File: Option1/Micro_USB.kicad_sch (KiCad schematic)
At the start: 10 parts, among them J1401 10118194-0001LF, U1401 CH340X

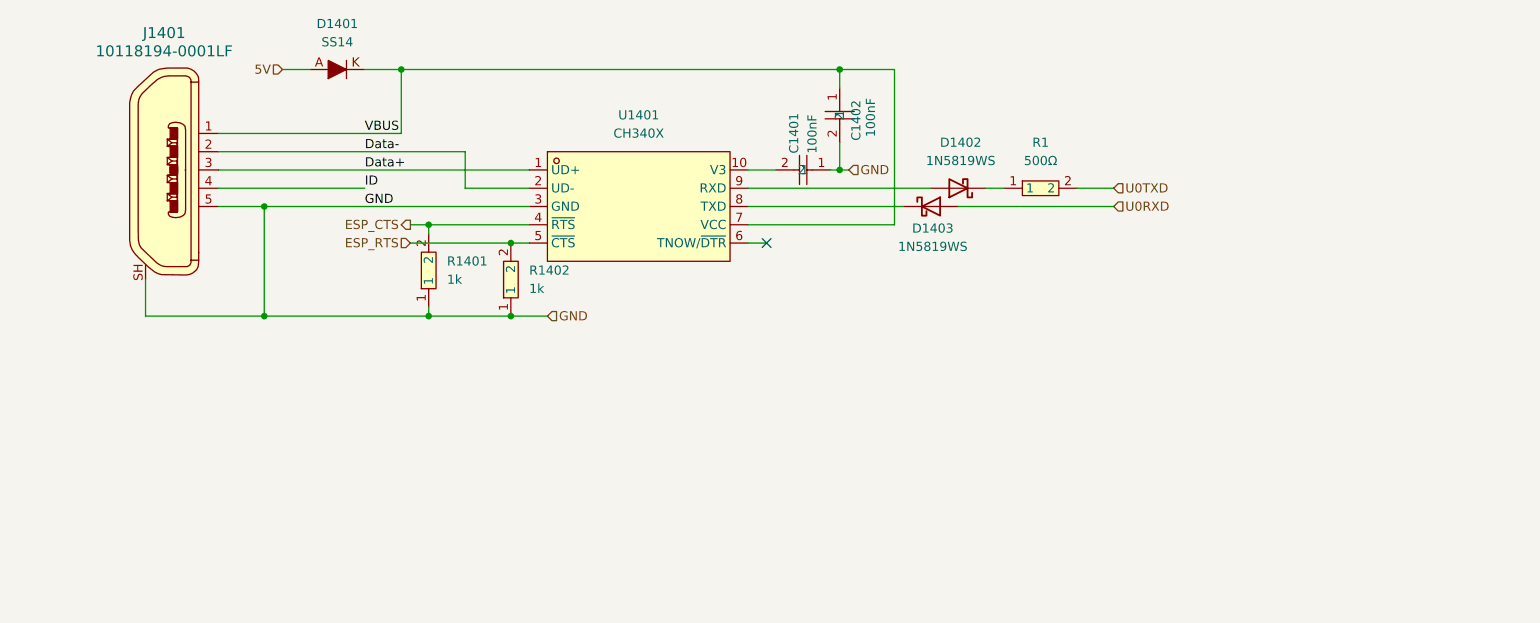
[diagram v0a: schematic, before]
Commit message: SPI Flash hinzugefügt, IN/Outputs vereinheitlicht, USB Flash Möglichkeit hinzugefügt, Display fehtl noch
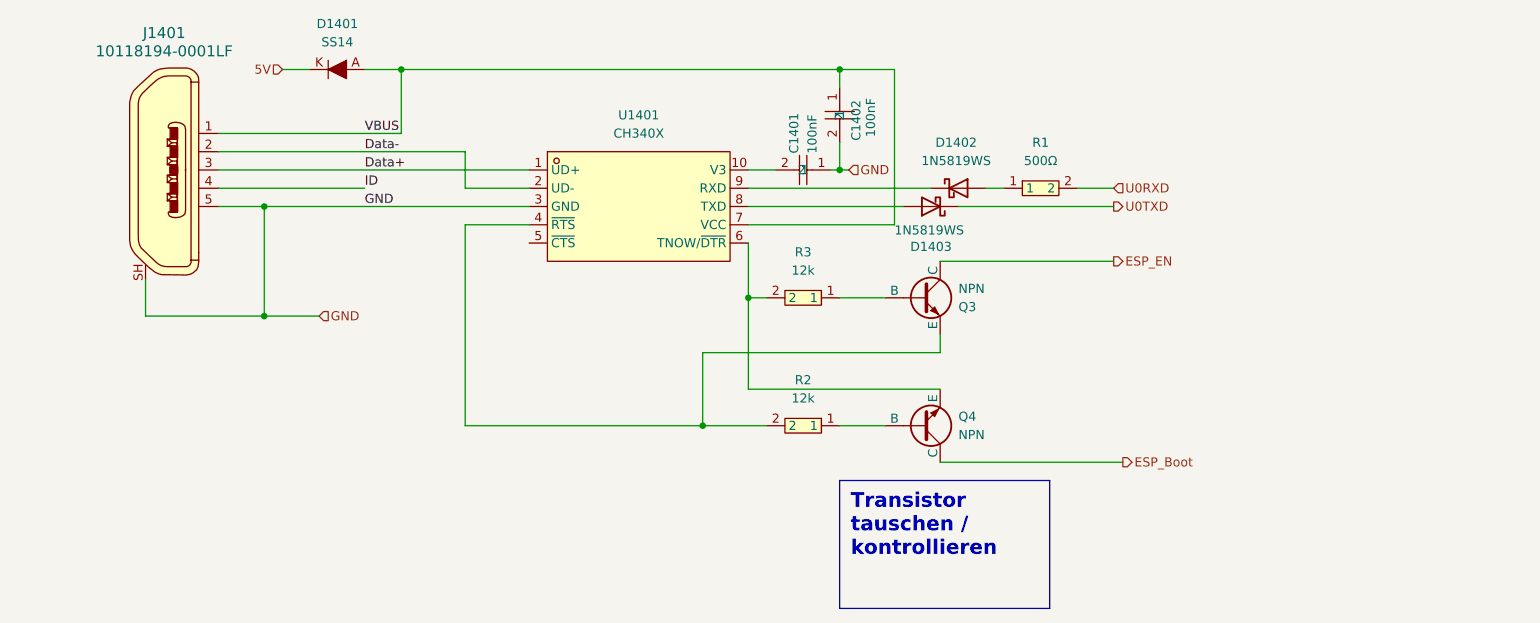
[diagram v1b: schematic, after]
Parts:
- removed R1401, R1402: 1k, easyeda2kicad:R0603, symbol easyeda2kicad:0603WAF1001T5E
- added Q3, Q4: NPN, symbol Simulation_SPICE:NPN
- added R2, R3: 12k, easyeda2kicad:R0603, symbol easyeda2kicad:0603WAF1202T5E
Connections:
- net 5V: now also D1401.K; no longer D1401.A
- net U0RXD: now also R1.2; no longer D1403.2 (A)
- net U0TXD: now also D1403.1 (K); no longer R1.2
- net VBUS: now also D1401.A; no longer D1401.K
- net at R1.1: now also D1402.2 (A); no longer D1402.1 (K)
- net at U1401.6 (TNOW/~{DTR}): now also Q4.3 (E), R3.2
- net at U1401.8 (TXD): now also D1403.2 (A); no longer D1403.1 (K)
- net at U1401.9 (RXD): now also D1402.1 (K); no longer D1402.2 (A)
- net ESP_CTS: no longer names the net of U1401.4 (~{RTS})
- net ESP_CTS: now also Q3.3 (E), R2.2
- net ESP_RTS: no longer names the net of U1401.5 (~{CTS})
- new net: Q3.2 (B), R3.1
- new net: Q4.2 (B), R2.1
- new net ESP_Boot: Q4.1 (C)
- new net ESP_EN: Q3.1 (C)
- no-connect marks 1 -> 0
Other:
- moved on the sheet: D1401, D1402, D1403

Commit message: Added Export for Review 1
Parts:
- renumbered Q3 to Q1401, Q4 to Q1402
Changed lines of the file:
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@@
 		(dnp no)
 		(fields_autoplaced yes)
-		(property "Reference" "Q3"
-			(at 149.86 69.8501 0)
+		(property "Reference" "Q1401"
+			(at 149.86 67.3099 0)
 			(effects
 				(font
@@
 		)
 		(property "Value" "NPN"
-			(at 149.86 67.3101 0)
+			(at 149.86 69.8499 0)
 			(effects
 				(font
@@
 			(project ""
 				(path "/b9e5f262-9648-4b79-bdd1-af888b822329/38430192-9545-4dc5-9188-f56f0a78c828"
-					(reference "Q3")
+					(reference "Q1401")
 					(unit 1)
 				)
@@
 		(dnp no)
 		(fields_autoplaced yes)
-		(property "Reference" "Q4"
+		(property "Reference" "Q1402"
 			(at 149.86 85.0899 0)
 			(effects
@@
 			(project ""
 				(path "/b9e5f262-9648-4b79-bdd1-af888b822329/38430192-9545-4dc5-9188-f56f0a78c828"
-					(reference "Q4")
+					(reference "Q1402")
 					(unit 1)
 				)

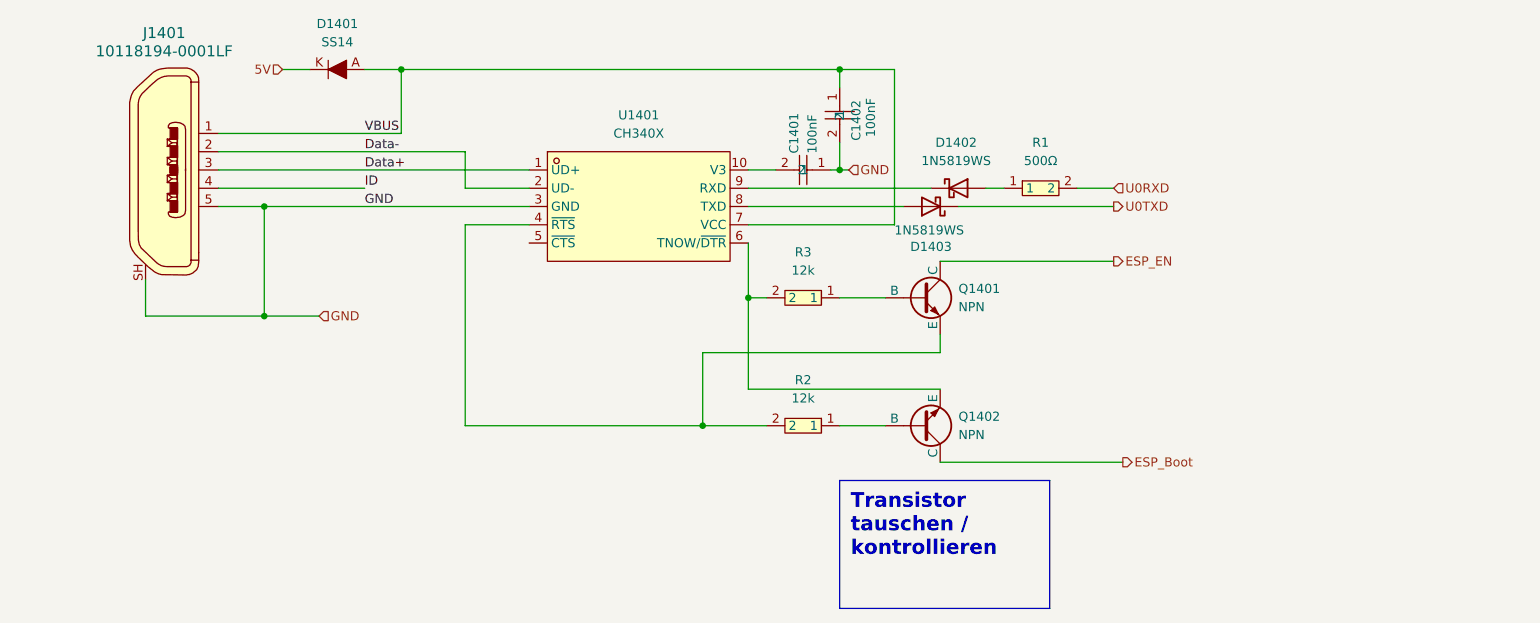
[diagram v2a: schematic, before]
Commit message: USB auf 3V3 umgebaut
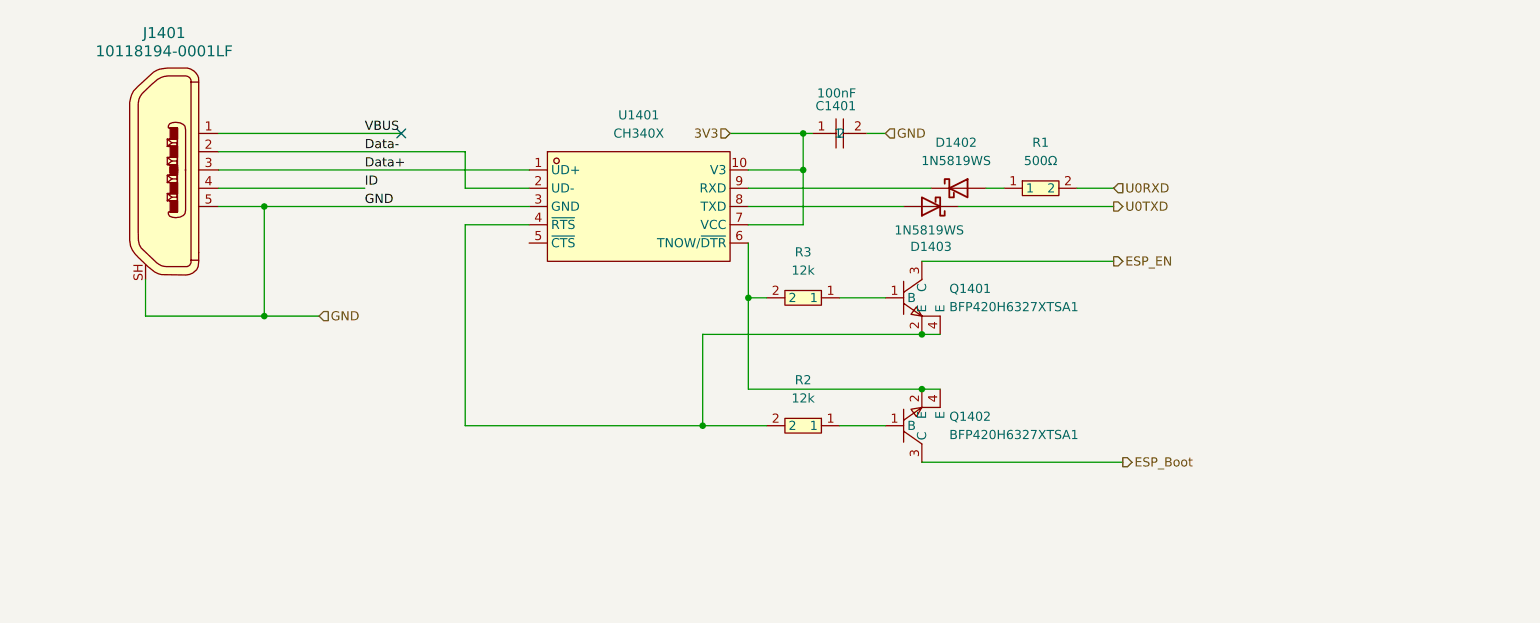
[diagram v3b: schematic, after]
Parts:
- removed C1401: 100nF, easyeda2kicad:C0603, symbol easyeda2kicad:CL10B104KA8NNNC
- removed D1401: SS14, digikey-footprints:DO-214AC, symbol dk_Diodes-Rectifiers-Single:SS14
- removed Q1401, Q1402: NPN, symbol Simulation_SPICE:NPN
- added Q1401, Q1402: BFP420H6327XTSA1, easyeda2kicad:SOT343_L2.0-W1.3-P1.30-LS2.1-BL, symbol EasyEda2KiCad:BFP420H6327XTSA1
- renumbered C1402 to C1401
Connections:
- net ESP_Boot: now also Q1402.3 (C)
- net ESP_EN: now also Q1401.3 (C)
- net VBUS: no longer C1401.1, U1401.7 (VCC)
- net 3V3: now reaches U1401.10 (V3)
- net 3V3: now also C1401.1, U1401.7 (VCC)
- net at R2.2, U1401.4 (~{RTS}): now also Q1401.2 (E), Q1401.4 (E)
- net at R3.2, U1401.6 (TNOW/~{DTR}): now also Q1402.2 (E), Q1402.4 (E)
- net at R3.1: now also Q1401.1 (B)
- net at R2.1: now also Q1402.1 (B)
- no-connect marks 0 -> 1
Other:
- moved on the sheet: C1401

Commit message: USB Schaltung angepasst, Transistoren korrigiert, Stecker ausgetauscht, Dioden hinzugefügt
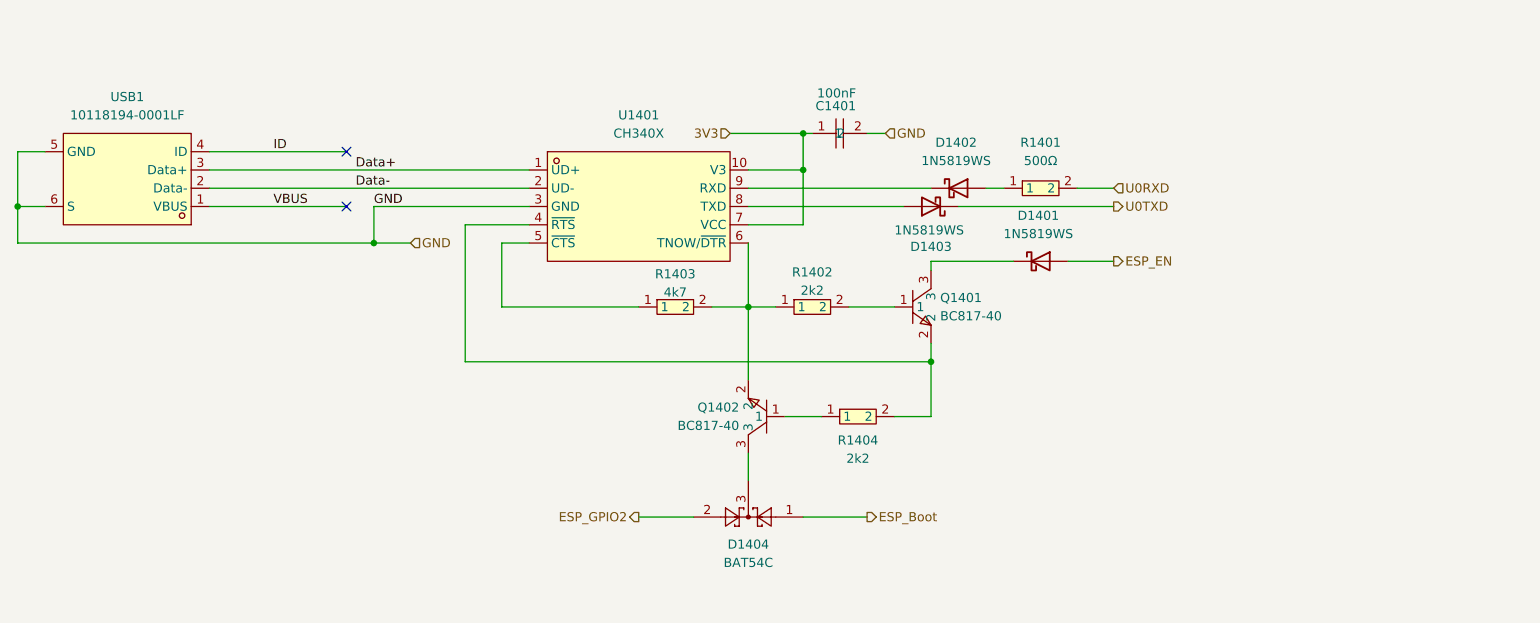
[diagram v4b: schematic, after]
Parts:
- removed J1401: 10118194-0001LF, digikey-footprints:USB_Micro_B_Female_10118194-0001LF, symbol dk_USB-DVI-HDMI-Connectors:10118194-0001LF
- removed Q1401, Q1402: BFP420H6327XTSA1, easyeda2kicad:SOT343_L2.0-W1.3-P1.30-LS2.1-BL, symbol EasyEda2KiCad:BFP420H6327XTSA1
- removed R2, R3: 12k, easyeda2kicad:R0603, symbol easyeda2kicad:0603WAF1202T5E
- added D1401: 1N5819WS, Diode_SMD:D_SOD-323, symbol Diode:1N5819WS
- added D1404: BAT54C, Package_TO_SOT_SMD:SOT-23, symbol Diode:BAT54C
- added Q1401, Q1402: BC817-40, easyeda2kicad:SOT-23-3_L2.9-W1.3-P1.90-LS2.4-BR, symbol easyeda2kicad:BC817-40
- added R1402, R1404: 2k2, easyeda2kicad:R0603, symbol easyeda2kicad:0603WAF2201T5E
- added R1403: 4k7, easyeda2kicad:R0603, symbol easyeda2kicad:0603WAF4701T5E
- added USB1: 10118194-0001LF, easyeda2kicad:MICRO-USB-SMD_10118194-0001LF, symbol easyeda2kicad:10118194-0001LF
- renumbered R1 to R1401
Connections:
- net Data+: now also USB1.3 (Data+)
- net Data-: now also USB1.2 (Data-)
- net ESP_Boot: now also D1404.1
- net ESP_EN: now also D1401.2 (A)
- net GND: now also USB1.5 (GND), USB1.6 (S)
- net ID: now also USB1.4 (ID)
- net VBUS: now also USB1.1 (VBUS)
- net at U1401.4 (~{RTS}): now also Q1401.2, R1404.2
- net at U1401.5 (~{CTS}): now also R1403.1
- net at U1401.6 (TNOW/~{DTR}): now also Q1402.2, R1402.1, R1403.2
- new net: Q1401.1, R1402.2
- new net: D1401.1 (K), Q1401.3
- new net: D1404.3, Q1402.3
- new net: Q1402.1, R1404.1
- new net ESP_GPIO2: D1404.2
- no-connect marks 1 -> 2

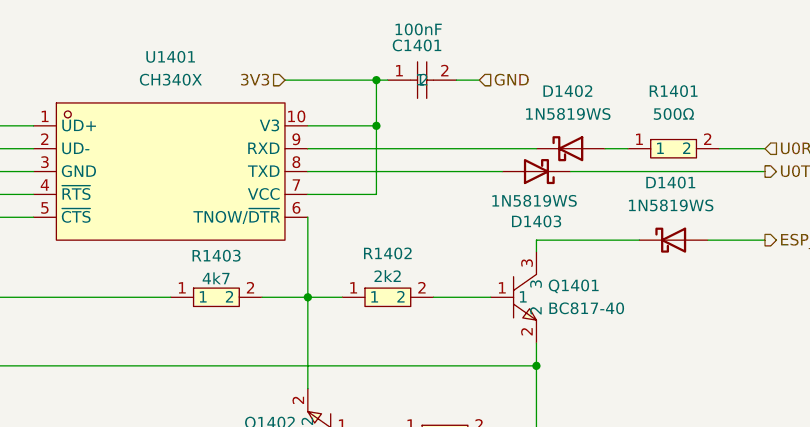
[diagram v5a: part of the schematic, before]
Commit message: EasyEDA Lib in Projekt verschoben; Footprints, Silkscreen für designrule angepasst; Bauteilbeschriftungen entfernt, müssen neu angeordnet werden, JLC Rules eingebunden, Designrules erfolgreich bis auf Beschriftungen, Fehler in Radio Controll Beschaltung behoben; RFID Pinheader hinzugefügt
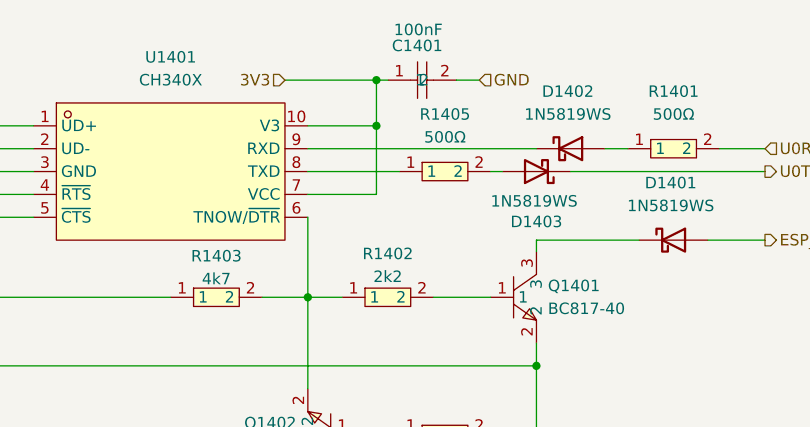
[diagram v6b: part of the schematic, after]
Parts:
- added R1405: 500Ω, easyeda2kicad:R0603, symbol easyeda2kicad:0603WAF4990T5E
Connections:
- net at U1401.8 (TXD): now also R1405.1; no longer D1403.2 (A)
- new net: D1403.2 (A), R1405.2
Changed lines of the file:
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@@
+	(wire
+		(pts
+			(xy 140.97 55.88) (xy 142.24 55.88)
+		)
+		(stroke
+			(width 0)
+			(type default)
+		)
+	)
 	(wire
 		(pts
@@
 	(wire
 		(pts
-			(xy 120.65 55.88) (xy 142.24 55.88)
+			(xy 120.65 55.88) (xy 130.81 55.88)
 		)
 		(stroke
@@
 					(unit 1)
 				)
+			)
+		)
+	)
+	(symbol
+		(lib_id "easyeda2kicad:0603WAF4990T5E")
+		(at 135.89 55.88 0)
+		(unit 1)
+		(exclude_from_sim no)
+		(in_bom yes)
+		(on_board yes)
+		(dnp no)
+		(fields_autoplaced yes)
+		(property "Reference" "R1405"
+			(at 135.89 49.53 0)
+			(effects
+				(font
+					(size 1.27 1.27)
+				)
+			)
+		)
+		(property "Value" "500Ω"
+			(at 135.89 52.07 0)
+			(effects
+				(font
+					(size 1.27 1.27)
+				)
+			)
+		)
+		(property "Footprint" "easyeda2kicad:R0603"
+			(at 135.89 63.5 0)
+			(effects
+				(font
+					(size 1.27 1.27)
+				)
+				(hide yes)
+			)
+		)
+		(property "Datasheet" "https://lcsc.com/product-detail/Chip-Resistor-Surface-Mount-UniOhm_499R-4990-1_C23065.html"
+			(at 135.89 66.04 0)
+			(effects
+				(font
+					(size 1.27 1.27)
+				)
+				(hide yes)
+			)
+		)
+		(property "Description" ""
+			(at 135.89 55.88 0)
+			(effects
+				(font
+					(size 1.27 1.27)
+				)
+				(hide yes)
+			)
+		)
+		(property "LCSC Part" "C23065"
+			(at 135.89 68.58 0)
+			(effects
+				(font
+					(size 1.27 1.27)
+				)
+				(hide yes)
+			)
+		)
+		(pin "1"
+		)
+		(pin "2"
+		)
+		(instances
+			(project "Option1"
+				(path "/b9e5f262-9648-4b79-bdd1-af888b822329/38430192-9545-4dc5-9188-f56f0a78c828"
+					(reference "R1405")
+					(unit 1)
+				)

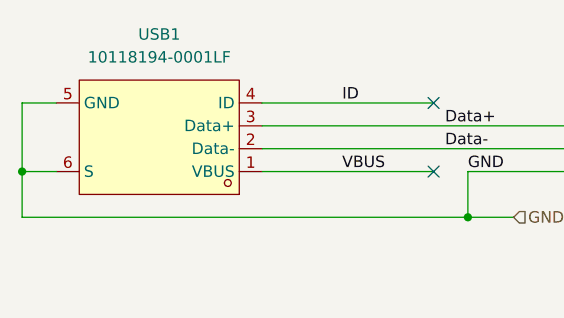
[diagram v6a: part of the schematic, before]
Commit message: BOM und Positionsdaten korrigiert
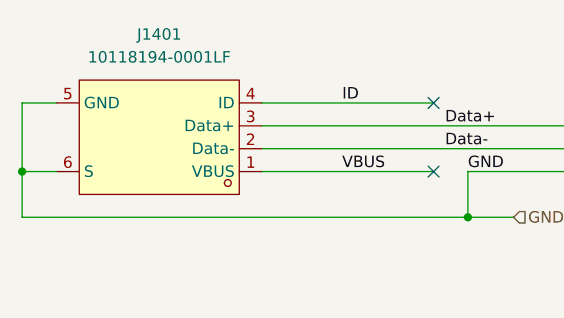
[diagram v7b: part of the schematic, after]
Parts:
- renumbered USB1 to J1401
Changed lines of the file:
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@@
 		(dnp no)
 		(fields_autoplaced yes)
-		(property "Reference" "USB1"
+		(property "Reference" "J1401"
 			(at 34.29 40.64 0)
 			(effects
@@
 			(project ""
 				(path "/b9e5f262-9648-4b79-bdd1-af888b822329/38430192-9545-4dc5-9188-f56f0a78c828"
-					(reference "USB1")
+					(reference "J1401")
 					(unit 1)
 				)
